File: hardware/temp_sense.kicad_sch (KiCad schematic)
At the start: 42 parts, among them U2 CD4052B, U3 LM324, U4 CD4052B, U5 LM324

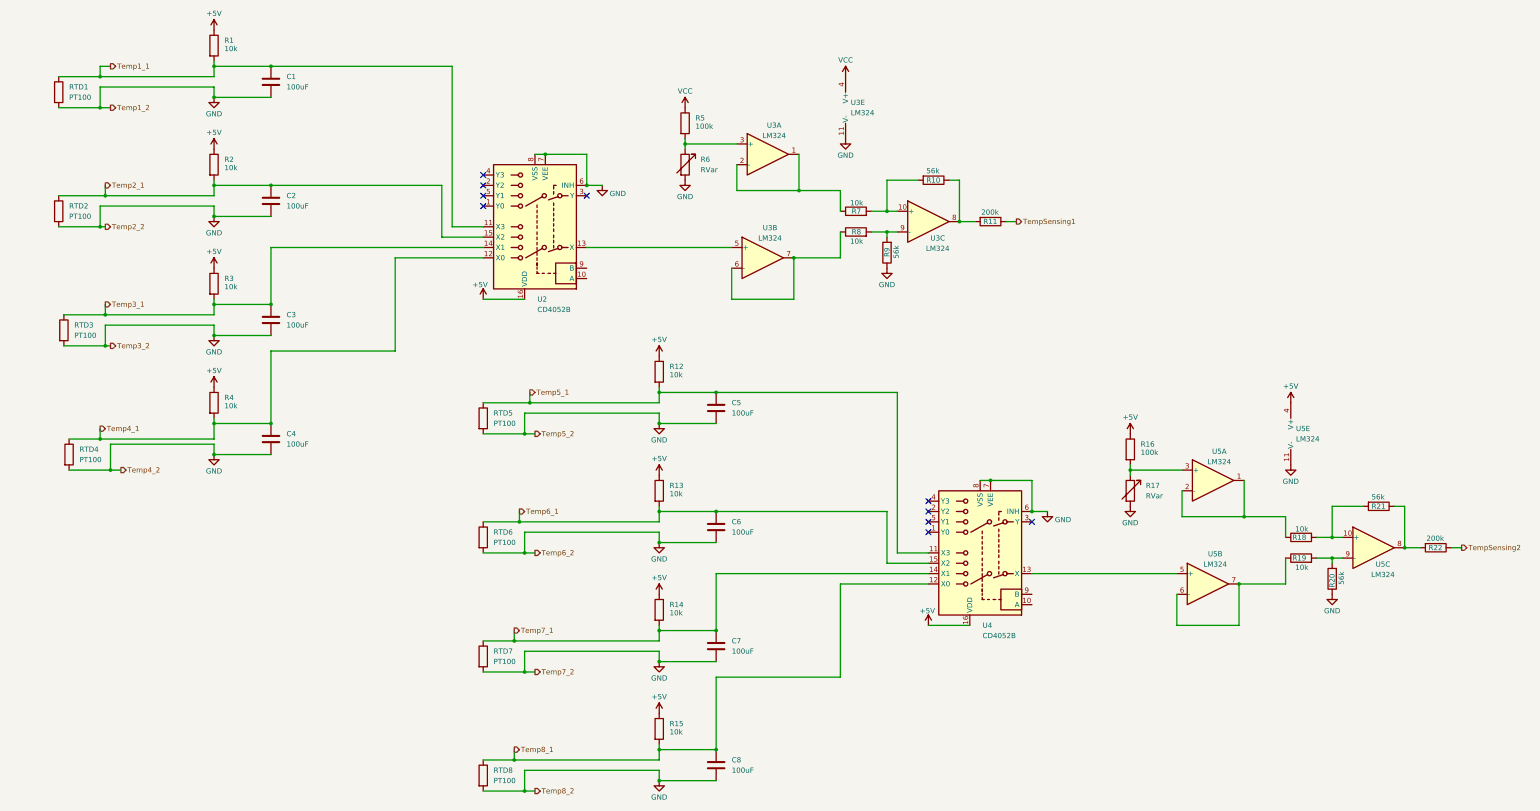
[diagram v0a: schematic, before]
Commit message: Pin assignment first draft
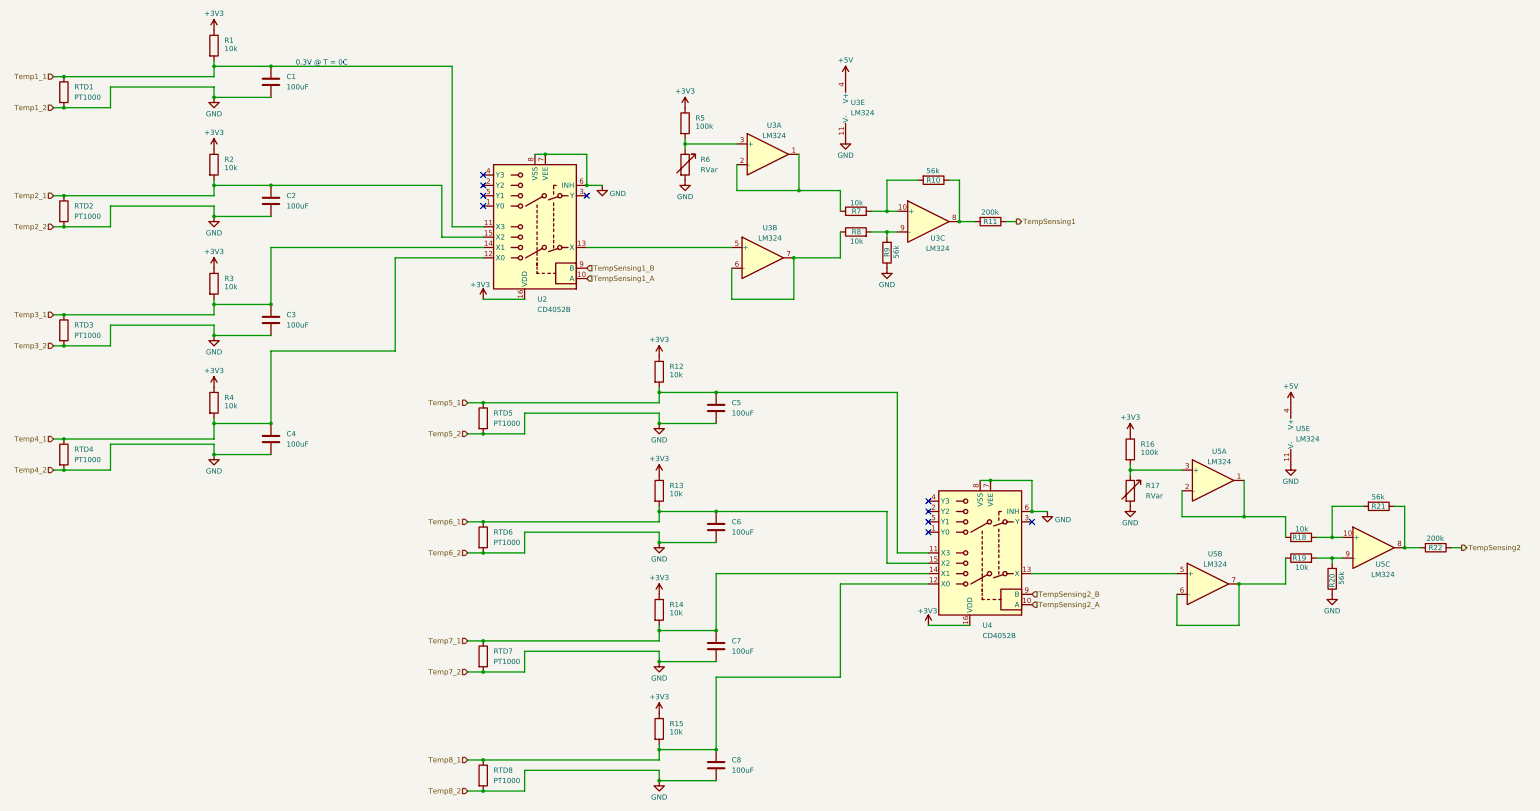
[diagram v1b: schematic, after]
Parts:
- RTD1, RTD2, RTD3, RTD4, RTD5, RTD6, RTD7, RTD8: value PT100 -> PT1000
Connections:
- net +5V: now also U3.4 (V+); no longer R1.1, R12.1, R13.1, R14.1, R15.1, R16.1, R2.1, R3.1, R4.1, U2.16 (VDD), U4.16 (VDD)
- net TempSensing2_A: now reaches U4.10 (A)
- net TempSensing2_B: now reaches U4.9 (B)
- net TempSensing1_A: now reaches U2.10 (A)
- net TempSensing1_B: now reaches U2.9 (B)
- net VCC renamed +3V3
- net +3V3: now also R1.1, R12.1, R13.1, R14.1, R15.1, R16.1, R2.1, R3.1, R4.1, U2.16 (VDD), U4.16 (VDD); no longer U3.4 (V+)
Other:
- note added: "0.3V @ T = 0C"
- moved on the sheet: RTD1, RTD2, RTD4
